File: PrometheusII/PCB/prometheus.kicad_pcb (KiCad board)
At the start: 4 copper layers, 223.5 x 222.3 mm, 225 parts, among them J1 0878311420, J10 Conn_02x02_Odd_Even, J11 Conn_02x02_Odd_Even, J12 Conn_02x08_Odd_Even, J13 Conn_02x08_Odd_Even, J14 Conn_02x08_Odd_Even, J2 Conn_02x08_Odd_Even, J3 Conn_02x02_Odd_Even, J4 Conn_02x02_Odd_Even, J7 Conn_02x08_Odd_Even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

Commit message: End of day checkpoint
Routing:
- net (no net): track 323.2 -> 400.0 mm
- net +3V3: track 179.5 -> 146.9 mm
- net /LEN_ATV_P: track 40.7 -> 18.4 mm
- net /LEN_CV_P: track 33.2 -> 20.7 mm
- net /LEN_KNOB_P: track 9.34 -> 1.85 mm
- net GND: track 316.3 -> 308.9 mm

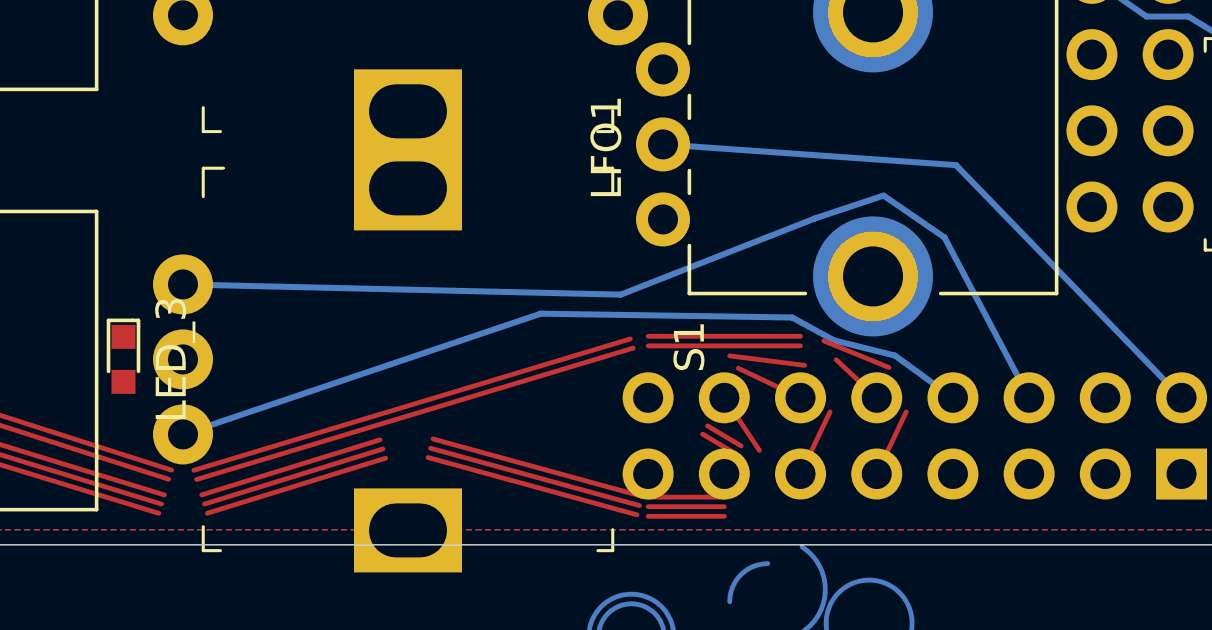
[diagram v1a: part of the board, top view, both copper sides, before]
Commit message: Update to use user units
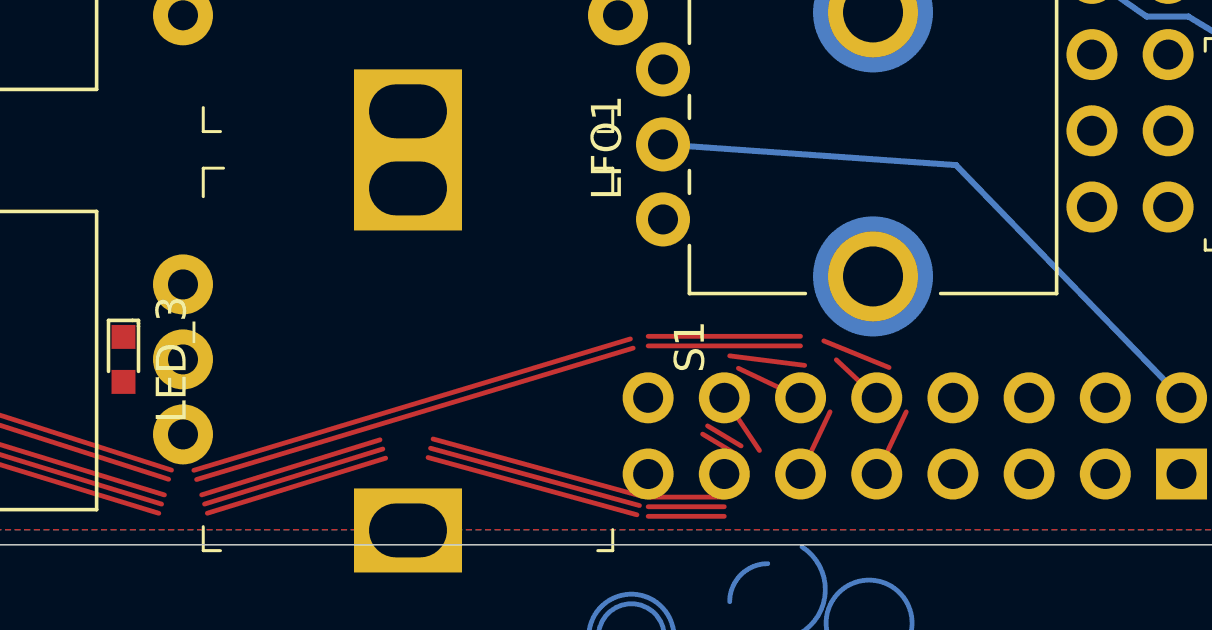
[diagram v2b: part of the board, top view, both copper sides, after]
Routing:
- net /VOCT_OCT_A_P: track 32.5 -> 0.00 mm
- net /VOCT_OCT_B_P: track 27.0 -> 0.00 mm
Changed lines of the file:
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@@
     (thickness 1.6)
     (drawings 152)
-    (tracks 643)
+    (tracks 633)
     (zones 0)
     (modules 225)
@@
   (segment (start 138.5435 104.806) (end 141.7935 109.556) (width 0.2) (layer B.Cu) (net 136))
   (segment (start 136.7935 104.806) (end 138.5435 104.806) (width 0.2) (layer B.Cu) (net 136))
-  (segment (start 105.41 124.47) (end 103.4795 123.063) (width 0.2) (layer B.Cu) (net 137))
-  (segment (start 103.4795 123.063) (end 101.4475 122.555) (width 0.2) (layer B.Cu) (net 137))
-  (segment (start 101.4475 122.555) (end 100.0505 121.793) (width 0.2) (layer B.Cu) (net 137))
-  (segment (start 100.0505 121.793) (end 91.6685 121.666) (width 0.2) (layer B.Cu) (net 137))
-  (segment (start 91.6685 121.666) (end 79.7455 125.69) (width 0.2) (layer B.Cu) (net 137))
-  (segment (start 107.95 124.47) (end 105.1305 119.126) (width 0.2) (layer B.Cu) (net 138))
-  (segment (start 105.1305 119.126) (end 103.0985 117.729) (width 0.2) (layer B.Cu) (net 138))
-  (segment (start 103.0985 117.729) (end 100.8125 118.491) (width 0.2) (layer B.Cu) (net 138))
-  (segment (start 100.8125 118.491) (end 94.3355 121.031) (width 0.2) (layer B.Cu) (net 138))
-  (segment (start 94.3355 121.031) (end 79.7455 120.69) (width 0.2) (layer B.Cu) (net 138))
   (zone (net 1) (net_name GND) (layer In2.Cu) (hatch edge 0.508)
     (connect_pads (clearance 0.16))

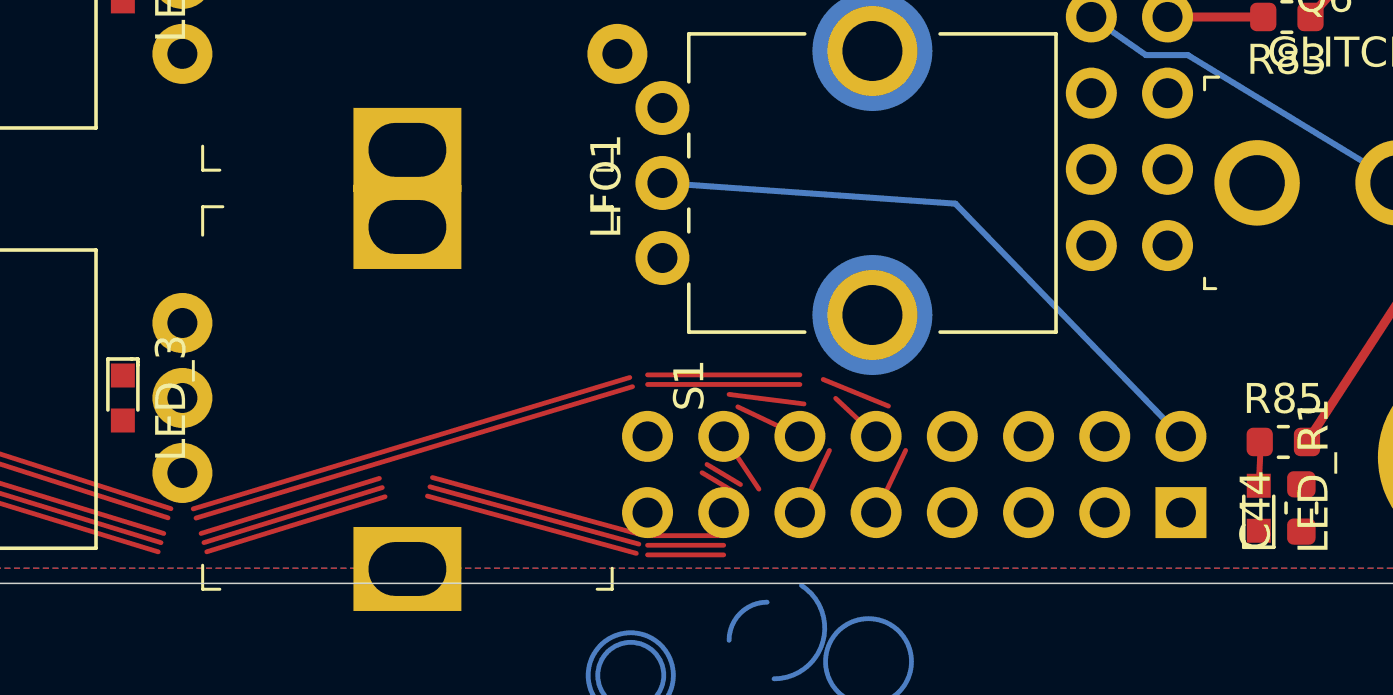
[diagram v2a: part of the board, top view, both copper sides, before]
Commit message: Updated to allow non-pad node centers
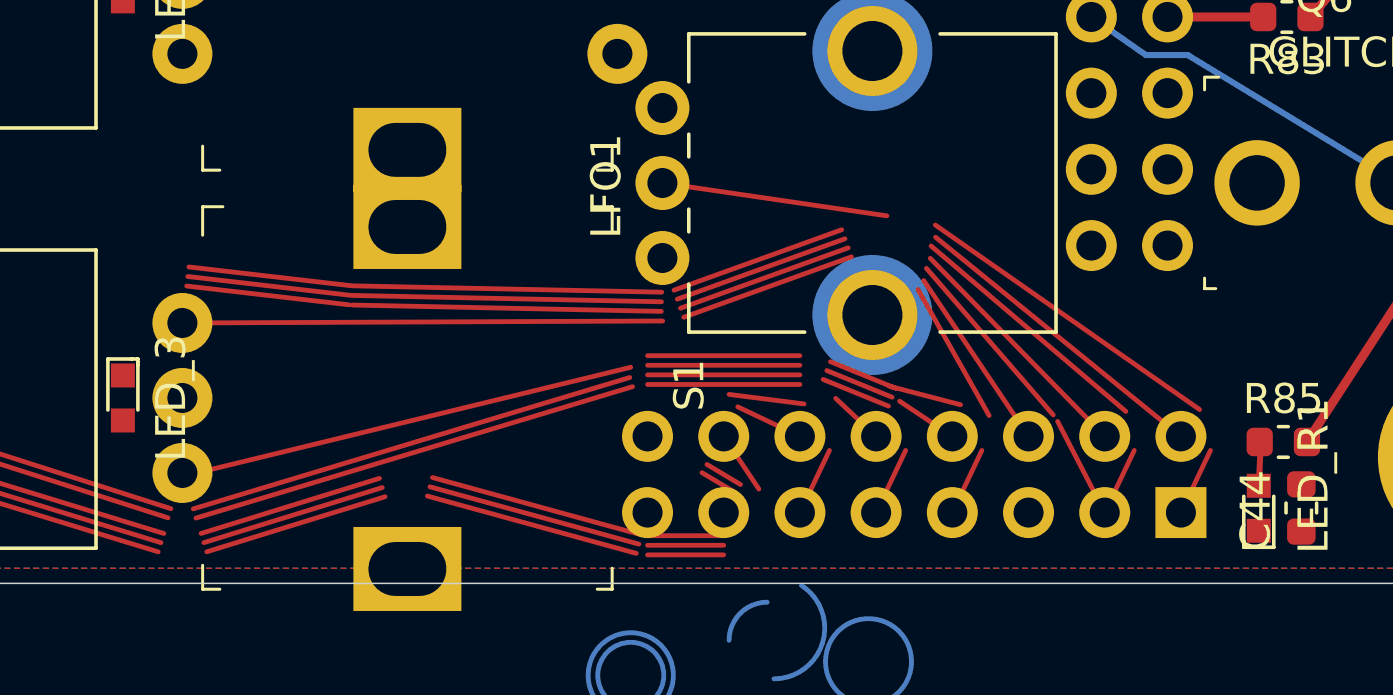
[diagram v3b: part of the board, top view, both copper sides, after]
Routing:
- net (no net): track 400.0 -> 514.1 mm
- net /VOCT_OCT_A_P: track 0.00 -> 22.3 mm
- net /VOCT_OCT_B_P: track 0.00 -> 17.2 mm
- net GND: track 308.9 -> 324.0 mm
- net /PARAM_1_P: track 0.00 -> 8.31 mm
- net /LFO_P: track 20.6 -> 18.1 mm
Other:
- board text added: "2020-04"
- board text removed: "2020-01"
- board text removed: "Prometheus II Rev 00"
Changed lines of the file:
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@@
   (general
     (thickness 1.6)
-    (drawings 152)
-    (tracks 633)
+    (drawings 180)
+    (tracks 661)
     (zones 0)
     (modules 225)
@@
     (solder_mask_min_width 0.25)
     (aux_axis_origin 156.456 180.632)
-    (grid_origin 102.87 127.01)
+    (grid_origin 79.9487 118.15)
     (visible_elements 7FFFFFFF)
     (pcbplotparams
@@
     )
   )
+  (gr_circle (center 85.4351 118.912) (end 86.6151 118.912) (layer B.SilkS) (width 0.16))
+  (gr_circle (center 85.4351 118.912) (end 86.2951 118.912) (layer B.SilkS) (width 0.16))
+  (gr_circle (center 85.4351 118.912) (end 85.9751 118.912) (layer B.SilkS) (width 0.16))
+  (gr_circle (center 79.7455 120.69) (end 81.6255 120.69) (layer B.SilkS) (width 0.16))
+  (gr_circle (center 79.7455 120.69) (end 81.3055 120.69) (layer B.SilkS) (width 0.16))
+  (gr_circle (center 79.7455 120.69) (end 80.9855 120.69) (layer B.SilkS) (width 0.16))
+  (gr_circle (center 95.746 118.524) (end 97.846 118.524) (layer B.SilkS) (width 0.16))
+  (gr_circle (center 95.746 118.524) (end 97.526 118.524) (layer B.SilkS) (width 0.16))
+  (gr_circle (center 95.746 118.524) (end 97.206 118.524) (layer B.SilkS) (width 0.16))
+  (gr_circle (center 95.746 118.524) (end 96.886 118.524) (layer B.SilkS) (width 0.16))
+  (gr_circle (center 102.746 120.424) (end 106.406 120.424) (layer B.SilkS) (width 0.16))
+  (gr_circle (center 113.03 124.47) (end 114.12 124.47) (layer B.SilkS) (width 0.16))
+  (gr_circle (center 110.49 124.47) (end 111.58 124.47) (layer B.SilkS) (width 0.16))
+  (gr_circle (center 107.95 124.47) (end 109.04 124.47) (layer B.SilkS) (width 0.16))
+  (gr_circle (center 105.41 124.47) (end 106.82 124.47) (layer B.SilkS) (width 0.16))
+  (gr_circle (center 102.746 120.424) (end 106.086 120.424) (layer B.SilkS) (width 0.16))
+  (gr_circle (center 102.746 120.424) (end 105.766 120.424) (layer B.SilkS) (width 0.16))
+  (gr_circle (center 102.746 120.424) (end 105.446 120.424) (layer B.SilkS) (width 0.16))
+  (gr_circle (center 102.746 120.424) (end 105.126 120.424) (layer B.SilkS) (width 0.16))
+  (gr_circle (center 102.746 120.424) (end 104.806 120.424) (layer B.SilkS) (width 0.16))
+  (gr_circle (center 102.746 120.424) (end 104.486 120.424) (layer B.SilkS) (width 0.16))
+  (gr_circle (center 105.41 124.47) (end 106.5 124.47) (layer B.SilkS) (width 0.16))
+  (gr_circle (center 102.87 124.47) (end 104.6 124.47) (layer B.SilkS) (width 0.16))
+  (gr_circle (center 102.87 124.47) (end 104.28 124.47) (layer B.SilkS) (width 0.16))
+  (gr_circle (center 95.25 124.47) (end 97.94 124.47) (layer B.SilkS) (width 0.16))
+  (gr_circle (center 95.25 124.47) (end 97.62 124.47) (layer B.SilkS) (width 0.16))
+  (gr_circle (center 100.33 124.47) (end 103.02 124.47) (layer B.SilkS) (width 0.16))
+  (gr_circle (center 100.33 124.47) (end 102.7 124.47) (layer B.SilkS) (width 0.16))
   (gr_circle (center 100.33 124.47) (end 101.42 124.47) (layer B.SilkS) (width 0.16))
   (gr_circle (center 102.87 124.47) (end 103.96 124.47) (layer B.SilkS) (width 0.16))
@@
     (effects (font (size 1 1) (thickness 0.15)) (justify left mirror))
   )
-  (gr_text "Prometheus II Rev 00" (at 105.5435 115.856) (layer B.SilkS)
+  (gr_text "Prometheus II Rev 01" (at 117.094 132.09) (layer B.SilkS)
     (effects (font (size 1 1) (thickness 0.15)) (justify mirror))
   )
-  (gr_text 2020-01 (at 110.0435 117.856) (layer B.SilkS)
+  (gr_text 2020-04 (at 121.92 133.614) (layer B.SilkS)
     (effects (font (size 1 1) (thickness 0.15)) (justify mirror))
   )
@@
   (segment (start 97.967637 123.071234) (end 100.467322 123.388684) (width 0.16) (layer F.Cu) (net 0))
   (segment (start 101.104803 122.572058) (end 103.281968 123.46085) (width 0.16) (layer F.Cu) (net 0))
+  (segment (start 101.225748 122.275795) (end 103.402913 123.164586) (width 0.16) (layer F.Cu) (net 0))
+  (segment (start 95.25 122.1) (end 100.33 122.1) (width 0.16) (layer F.Cu) (net 0))
+  (segment (start 95.25 121.78) (end 100.33 121.78) (width 0.16) (layer F.Cu) (net 0))
+  (segment (start 103.305905 122.795817) (end 105.684645 123.415168) (width 0.16) (layer F.Cu) (net 1))
+  (segment (start 101.346692 121.979531) (end 103.523858 122.868322) (width 0.16) (layer F.Cu) (net 1))
+  (segment (start 104.261077 119.568348) (end 106.637735 123.776627) (width 0.16) (layer F.Cu) (net 0))
+  (segment (start 104.546285 118.867281) (end 108.7745 123.757048) (width 0.16) (layer F.Cu) (net 0))
+  (segment (start 104.7012 118.12235) (end 111.195685 123.639272) (width 0.16) (layer F.Cu) (net 0))
+  (segment (start 104.841278 117.423098) (end 113.654003 123.576289) (width 0.16) (layer F.Cu) (net 0))
+  (segment (start 96.457735 120.49971) (end 102.047821 118.485922) (width 0.16) (layer F.Cu) (net 0))
+  (segment (start 101.939366 118.184861) (end 96.34928 120.198649) (width 0.16) (layer F.Cu) (net 0))
+  (segment (start 101.830911 117.8838) (end 96.240825 119.897589) (width 0.16) (layer F.Cu) (net 0))
+  (segment (start 101.722456 117.58274) (end 96.13237 119.596528) (width 0.16) (layer F.Cu) (net 0))
+  (segment (start 95.722551 119.663758) (end 85.423992 119.451885) (width 0.16) (layer F.Cu) (net 0))
+  (segment (start 95.715969 119.983691) (end 85.41741 119.771818) (width 0.16) (layer F.Cu) (net 0))
+  (segment (start 95.709387 120.303623) (end 85.410828 120.09175) (width 0.16) (layer F.Cu) (net 0))
+  (segment (start 79.887985 119.458213) (end 85.299509 120.084183) (width 0.16) (layer F.Cu) (net 0))
+  (segment (start 79.924755 119.140333) (end 85.336279 119.766303) (width 0.16) (layer F.Cu) (net 0))
+  (segment (start 79.961525 118.822452) (end 85.37305 119.448423) (width 0.16) (layer F.Cu) (net 0))
+  (segment (start 95.754659 120.623982) (end 79.7455 120.69) (width 0.16) (layer F.Cu) (net 138))
+  (segment (start 103.229644 117.119202) (end 95.746 116.024) (width 0.16) (layer F.Cu) (net 81))
+  (segment (start 114.014532 124.937755) (end 113.03 127.01) (width 0.16) (layer F.Cu) (net 1))
+  (segment (start 104.850983 117.830808) (end 113.03 124.47) (width 0.16) (layer F.Cu) (net 81))
+  (segment (start 104.674612 118.534435) (end 110.49 124.47) (width 0.16) (layer F.Cu) (net 85))
+  (segment (start 108.918283 123.969472) (end 110.49 127.01) (width 0.16) (layer F.Cu) (net 1))
+  (segment (start 111.474532 124.937755) (end 110.49 127.01) (width 0.16) (layer F.Cu) (net 1))
+  (segment (start 104.455321 119.274294) (end 107.95 124.47) (width 0.16) (layer F.Cu) (net 138))
+  (segment (start 94.689538 122.167222) (end 80.01 125.74) (width 0.16) (layer F.Cu) (net 137))
+  (segment (start 106.394532 124.937755) (end 105.41 127.01) (width 0.16) (layer F.Cu) (net 1))
+  (segment (start 103.652716 123.297202) (end 105.41 124.47) (width 0.16) (layer F.Cu) (net 137))
   (segment (start 103.854532 124.937755) (end 102.87 127.01) (width 0.16) (layer F.Cu) (net 1))
   (segment (start 101.314532 124.937755) (end 100.33 127.01) (width 0.16) (layer F.Cu) (net 1))
@@
   (segment (start 113.2585 111.76) (end 111.8615 111.76) (width 0.2) (layer B.Cu) (net 79))
   (segment (start 101.521968 123.202399) (end 102.87 124.47) (width 0.16) (layer F.Cu) (net 80))
-  (segment (start 105.5115 116.713) (end 113.03 124.47) (width 0.2) (layer B.Cu) (net 81))
-  (segment (start 95.746 116.024) (end 105.5115 116.713) (width 0.2) (layer B.Cu) (net 81))
   (segment (start 112.5835 110.489) (end 115.773 110.49) (width 0.3) (layer F.Cu) (net 82))
   (segment (start 104.1145 100.203) (end 110.49 93.98) (width 0.2) (layer B.Cu) (net 83))

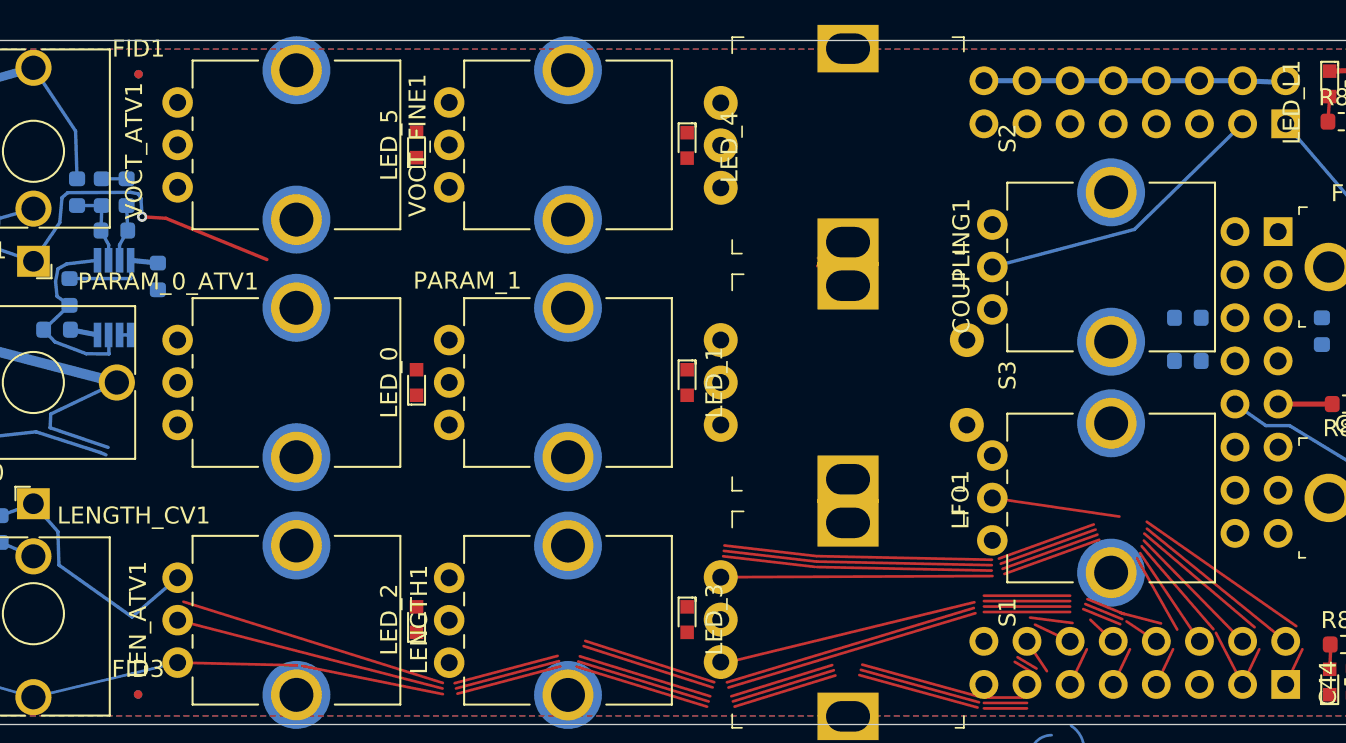
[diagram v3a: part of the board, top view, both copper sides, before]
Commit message: Placed new capacitors
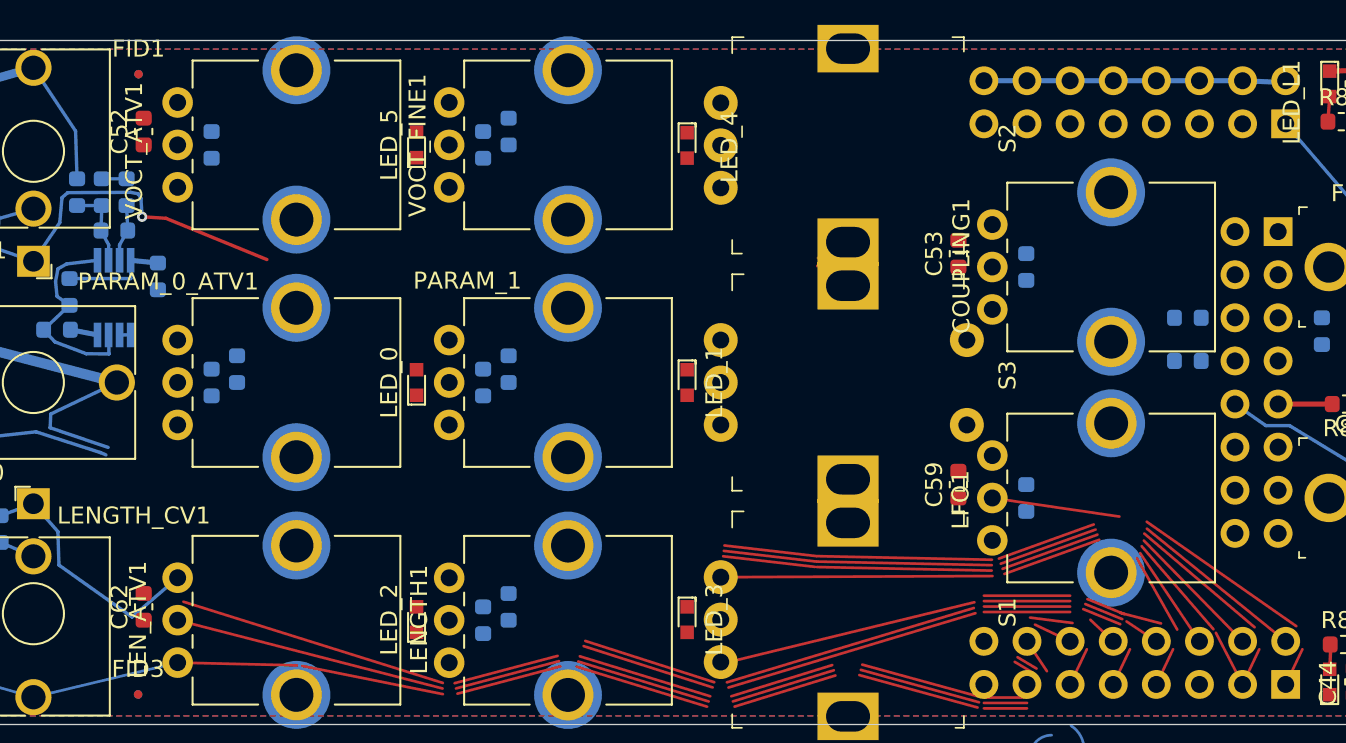
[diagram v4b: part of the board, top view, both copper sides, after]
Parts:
- added C25: 100n, Capacitor_SMD:C_0603_1608Metric, B.Cu at (65.7, 95.2)
- added C43: 100n, Capacitor_SMD:C_0603_1608Metric, B.Cu at (49.7, 95.2)
- added C50: 100n, Capacitor_SMD:C_0603_1608Metric, B.Cu at (97.7, 102.4)
- added C51: 1n, Capacitor_SMD:C_0603_1608Metric, B.Cu at (67.2, 94.4)
- added C52: 1n, Capacitor_SMD:C_0603_1608Metric, F.Cu at (45.7, 94.4)
- added C53: 1n, Capacitor_SMD:C_0603_1608Metric, F.Cu at (93.7, 101.6)
- added C54: 100n, Capacitor_SMD:C_0603_1608Metric, B.Cu at (65.7, 109.2)
- added C55: 100n, Capacitor_SMD:C_0603_1608Metric, B.Cu at (49.7, 109.2)
- added C56: 100n, Capacitor_SMD:C_0603_1608Metric, B.Cu at (97.7, 116.0)
- added C57: 1n, Capacitor_SMD:C_0603_1608Metric, B.Cu at (67.2, 108.4)
- added C58: 1n, Capacitor_SMD:C_0603_1608Metric, B.Cu at (51.2, 108.4)
- added C59: 1n, Capacitor_SMD:C_0603_1608Metric, F.Cu at (93.7, 115.2)
- added C60: 100n, Capacitor_SMD:C_0603_1608Metric, B.Cu at (65.7, 123.2)
- added C61: 1n, Capacitor_SMD:C_0603_1608Metric, B.Cu at (67.2, 122.4)
- added C62: 1n, Capacitor_SMD:C_0603_1608Metric, F.Cu at (45.7, 122.4)
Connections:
- H7 pad 1: (no net) -> GND (x2)
- LENGTH1 pad : GND -> (no net)
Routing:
- net /CV_FILT_P: track 17.6 -> 0.00 mm
